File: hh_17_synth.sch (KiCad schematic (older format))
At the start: 50 parts, among them J1 USB_OTG, J2 serial, J3 JACK_TRS, J4 SCL, J5 SDA, J6 out, SW2 SW_Push, SW3 SW_Push, U1 LM1117-3.3, U2 STM32F072CBTx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

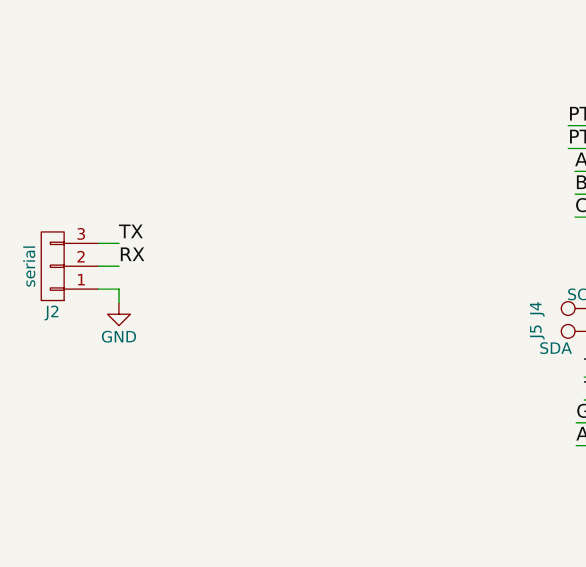
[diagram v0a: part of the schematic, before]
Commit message: changed uart conn to 2 pin (no gnd) misc layout improvements.
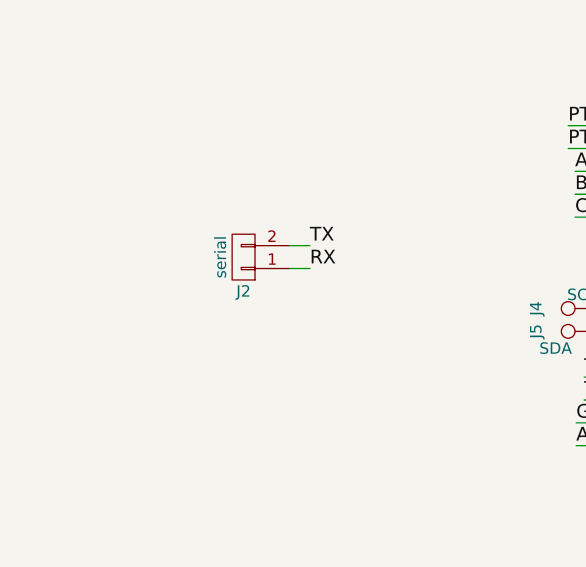
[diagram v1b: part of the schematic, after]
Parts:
- removed J2: serial, Pin_Headers:Pin_Header_Straight_1x03_Pitch2.54mm, symbol CONN_01X03
- added J2: serial, Pin_Headers:Pin_Header_Straight_1x02_Pitch2.54mm, symbol CONN_01X02
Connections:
- net RX: now also J2.1 (P1)
- net TX: now also J2.2 (P2)
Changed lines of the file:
@@
 Wire Wire Line
 	6815 7060 6355 7060
-$Comp
-L CONN_01X03 J2
-U 1 1 58FE2AF3
-P 1275 4400
-F 0 "J2" H 1275 4600 50  0000 C CNN
-F 1 "serial" V 1375 4400 50  0000 C CNN
-F 2 "Pin_Headers:Pin_Header_Straight_1x03_Pitch2.54mm" H 1275 4400 50  0001 C CNN
-F 3 "" H 1275 4400 50  0001 C CNN
-	1    1275 4400
-	-1   0    0    1
-$EndComp
 Wire Wire Line
-	1475 4300 1565 4300
-Text Label 1565 4300 0    60   ~ 0
+	2310 4310 2400 4310
+Text Label 2400 4310 0    60   ~ 0
 TX
 Wire Wire Line
-	1475 4400 1565 4400
-Text Label 1565 4400 0    60   ~ 0
+	2310 4410 2400 4410
+Text Label 2400 4410 0    60   ~ 0
 RX
-Wire Wire Line
-	1475 4500 1565 4500
-Wire Wire Line
-	1565 4500 1565 4560
-$Comp
-L GND #PWR036
-U 1 1 58FE33E7
-P 1565 4560
-F 0 "#PWR036" H 1565 4310 50  0001 C CNN
-F 1 "GND" H 1565 4410 50  0000 C CNN
-F 2 "" H 1565 4560 50  0001 C CNN
-F 3 "" H 1565 4560 50  0001 C CNN
-	1    1565 4560
-	1    0    0    -1
-$EndComp
 Wire Wire Line
 	4010 7300 4075 7300
@@
 Wire Wire Line
 	12415 5285 12275 5285
+$Comp
+L CONN_01X02 J2
+U 1 1 58FE5661
+P 2110 4360
+F 0 "J2" H 2110 4510 50  0000 C CNN
+F 1 "serial" V 2210 4360 50  0000 C CNN
+F 2 "Pin_Headers:Pin_Header_Straight_1x02_Pitch2.54mm" H 2110 4360 50  0001 C CNN
+F 3 "" H 2110 4360 50  0001 C CNN
+	1    2110 4360
+	-1   0    0    1
+$EndComp
 $EndSCHEMATC
